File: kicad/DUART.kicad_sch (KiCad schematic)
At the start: 1 part

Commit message: Lot of stuff. Memmory decoder in GAL Added README for Digital Updated sketch for Arduino
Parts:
- added C? (x2): C, symbol Device:C
- added U?: 74LS245, symbol 74xx:74LS245
- added U?: 74LS244, symbol 74xx:74LS244
- added Y?: Crystal, symbol Device:Crystal
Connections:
- net RS1: now reaches U?.1 (RS1)
- net RS1: now also U?.3 (RS2), U?.5 (RS3), U?.6 (RS4), U?.12 (O3a), U?.14 (O2a), U?.16 (O1a), U?.18 (O0a)
- net D1: now reaches U?.16 (D1)
- net D1: now also U?.8 (A6)
- net D3: now reaches U?.17 (D3)
- net D3: now also U?.6 (A4)
- net D5: now reaches U?.18 (D5)
- net D5: now also U?.4 (A2)
- net D7: now reaches U?.19 (D7)
- net D7: now also U?.2 (A0)
- net D6: now reaches U?.22 (D6)
- net D6: now also U?.3 (A1)
- net D4: now reaches U?.23 (D4)
- net D4: now also U?.5 (A3)
- net D2: now reaches U?.24 (D2)
- net D2: now also U?.7 (A5)
- net D0: now reaches U?.25 (D0)
- net D0: now also U?.9 (A7)
- net at U?.32 (X1/CLK): now also C?.2, Y?.1
- net at U?.33 (X2): now also C?.2, Y?.2
- net VCC: now reaches U?.40 (VCC)
- net VCC: now also U?.19 (OEb), U?.20 (VCC), U?.20 (VCC)
- net DUART_R/W: now reaches U?.8 (R/W)
- new net GND: C?.1, C?.1, U?.10 (GND)

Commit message: KiCad updates
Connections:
- net DUART_R/W is gone; now on net ~{ODDWRITE}: U?.8 (R/W)
- net GND: now also U?.11 (I0b), U?.13 (I1b), U?.15 (I2b), U?.17 (I3b), U?.3 (O3b), U?.5 (O2b), U?.7 (O1b), U?.9 (O0b)
- net ~{DUARTSEL}: now reaches U?.35 (CS)
- net ~{DUARTSEL}: now also U?.1 (OEa), U?.19 (CE)
- net ~{ODDWRITE}: now reaches U?.1 (A->B)
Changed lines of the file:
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@@
 (kicad_sch (version 20211123) (generator eeschema)
   (paper "A4")
+  (junction (at 38.1 134.62) (diameter 0) (color 0 0 0 0)
+  )
+  (junction (at 38.1 132.08) (diameter 0) (color 0 0 0 0)
+  )
+  (junction (at 71.12 132.08) (diameter 0) (color 0 0 0 0)
+  )
   (junction (at 93.98 44.45) (diameter 0) (color 0 0 0 0)
   )
+  (junction (at 38.1 137.16) (diameter 0) (color 0 0 0 0)
+  )
   (junction (at 104.14 44.45) (diameter 0) (color 0 0 0 0)
   )
+  (junction (at 71.12 134.62) (diameter 0) (color 0 0 0 0)
+  )
+  (junction (at 71.12 137.16) (diameter 0) (color 0 0 0 0)
+  )
   (bus_entry (at 105.41 71.12) (size 2.54 -2.54)
     (stroke (width 0) (type default) (color 0 0 0 0))
@@
     (stroke (width 0) (type default) (color 0 0 0 0))
   )
+  (wire (pts (xy 67.31 137.16) (xy 71.12 137.16))
+    (stroke (width 0) (type default) (color 0 0 0 0))
+  )
   (bus (pts (xy 105.41 93.98) (xy 105.41 91.44))
     (stroke (width 0) (type default) (color 0 0 0 0))
   )
+  (wire (pts (xy 71.12 134.62) (xy 71.12 137.16))
+    (stroke (width 0) (type default) (color 0 0 0 0))
+  )
+  (wire (pts (xy 71.12 129.54) (xy 71.12 132.08))
+    (stroke (width 0) (type default) (color 0 0 0 0))
+  )
   (wire (pts (xy 107.95 66.04) (xy 116.84 66.04))
     (stroke (width 0) (type default) (color 0 0 0 0))
@@
     (stroke (width 0) (type default) (color 0 0 0 0))
   )
+  (wire (pts (xy 67.31 134.62) (xy 71.12 134.62))
+    (stroke (width 0) (type default) (color 0 0 0 0))
+  )
   (bus (pts (xy 105.41 73.66) (xy 105.41 76.2))
     (stroke (width 0) (type default) (color 0 0 0 0))
@@
     (stroke (width 0) (type default) (color 0 0 0 0))
   )
+  (wire (pts (xy 67.31 132.08) (xy 71.12 132.08))
+    (stroke (width 0) (type default) (color 0 0 0 0))
+  )
+  (wire (pts (xy 71.12 137.16) (xy 72.39 137.16))
+    (stroke (width 0) (type default) (color 0 0 0 0))
+  )
   (bus (pts (xy 105.41 68.58) (xy 105.41 71.12))
     (stroke (width 0) (type default) (color 0 0 0 0))
@@
     (stroke (width 0) (type default) (color 0 0 0 0))
   )
-  (wire (pts (xy 107.95 101.6) (xy 116.84 101.6))
+  (wire (pts (xy 38.1 134.62) (xy 38.1 137.16))
     (stroke (width 0) (type default) (color 0 0 0 0))
   )
@@
     (stroke (width 0) (type default) (color 0 0 0 0))
   )
+  (wire (pts (xy 36.83 137.16) (xy 38.1 137.16))
+    (stroke (width 0) (type default) (color 0 0 0 0))
+  )
   (bus (pts (xy 105.41 71.12) (xy 105.41 73.66))
     (stroke (width 0) (type default) (color 0 0 0 0))
@@
     (stroke (width 0) (type default) (color 0 0 0 0))
   )
+  (wire (pts (xy 38.1 134.62) (xy 41.91 134.62))
+    (stroke (width 0) (type default) (color 0 0 0 0))
+  )
   (wire (pts (xy 104.14 25.4) (xy 104.14 29.21))
     (stroke (width 0) (type default) (color 0 0 0 0))
@@
     (stroke (width 0) (type default) (color 0 0 0 0))
   )
+  (wire (pts (xy 67.31 129.54) (xy 71.12 129.54))
+    (stroke (width 0) (type default) (color 0 0 0 0))
+  )
   (bus (pts (xy 78.74 121.92) (xy 78.74 124.46))
     (stroke (width 0) (type default) (color 0 0 0 0))
   )
+  (wire (pts (xy 38.1 137.16) (xy 41.91 137.16))
+    (stroke (width 0) (type default) (color 0 0 0 0))
+  )
   (wire (pts (xy 93.98 44.45) (xy 93.98 58.42))
     (stroke (width 0) (type default) (color 0 0 0 0))
   )
+  (wire (pts (xy 38.1 132.08) (xy 41.91 132.08))
+    (stroke (width 0) (type default) (color 0 0 0 0))
+  )
   (bus (pts (xy 78.74 68.58) (xy 78.74 66.04))
     (stroke (width 0) (type default) (color 0 0 0 0))
   )
+  (wire (pts (xy 38.1 132.08) (xy 38.1 134.62))
+    (stroke (width 0) (type default) (color 0 0 0 0))
+  )
   (wire (pts (xy 104.14 44.45) (xy 104.14 55.88))
     (stroke (width 0) (type default) (color 0 0 0 0))
@@
     (stroke (width 0) (type default) (color 0 0 0 0))
   )
+  (wire (pts (xy 38.1 129.54) (xy 38.1 132.08))
+    (stroke (width 0) (type default) (color 0 0 0 0))
+  )
   (wire (pts (xy 107.95 76.2) (xy 116.84 76.2))
     (stroke (width 0) (type default) (color 0 0 0 0))
   )
+  (wire (pts (xy 41.91 129.54) (xy 38.1 129.54))
+    (stroke (width 0) (type default) (color 0 0 0 0))
+  )
   (bus (pts (xy 105.41 96.52) (xy 105.41 93.98))
     (stroke (width 0) (type default) (color 0 0 0 0))
@@
     (stroke (width 0) (type default) (color 0 0 0 0))
   )
+  (wire (pts (xy 71.12 132.08) (xy 71.12 134.62))
+    (stroke (width 0) (type default) (color 0 0 0 0))
+  )
   (wire (pts (xy 104.14 44.45) (xy 102.87 44.45))
     (stroke (width 0) (type default) (color 0 0 0 0))
@@
     )
   )
-  (global_label "DUART_R{slash}W" (shape input) (at 107.95 101.6 180) (fields_autoplaced)
+  (global_label "~{DUARTSEL}" (shape input) (at 116.84 99.06 180) (fields_autoplaced)
     (effects (font (size 1.27 1.27)) (justify right))
-    (property "Intersheet References" "${INTERSHEET_REFS}" (id 0) (at 94.5907 101.5206 0)
+    (property "Intersheet References" "${INTERSHEET_REFS}" (id 0) (at 105.1136 99.1394 0)
       (effects (font (size 1.27 1.27)) (justify right) hide)
     )
@@
     )
   )
+  (global_label "~{ODDWRITE}" (shape input) (at 116.84 101.6 180) (fields_autoplaced)
+    (effects (font (size 1.27 1.27)) (justify right))
+    (property "Intersheet References" "${INTERSHEET_REFS}" (id 0) (at 105.1136 101.5206 0)
+      (effects (font (size 1.27 1.27)) (justify right) hide)
+    )
+  )
   (global_label "D6" (shape bidirectional) (at 35.56 78.74 0) (fields_autoplaced)
     (effects (font (size 1.27 1.27)) (justify left))
@@
     )
   )
+  (global_label "~{DUARTSEL}" (shape input) (at 41.91 142.24 180) (fields_autoplaced)
+    (effects (font (size 1.27 1.27)) (justify right))
+    (property "Intersheet References" "${INTERSHEET_REFS}" (id 0) (at 30.1836 142.3194 0)
+      (effects (font (size 1.27 1.27)) (justify right) hide)
+    )
+  )
+  (global_label "~{DUARTSEL}" (shape input) (at 67.31 55.88 0) (fields_autoplaced)
+    (effects (font (size 1.27 1.27)) (justify left))
+    (property "Intersheet References" "${INTERSHEET_REFS}" (id 0) (at 79.0364 55.8006 0)
+      (effects (font (size 1.27 1.27)) (justify left) hide)
+    )
+  )
   (global_label "A4" (shape output) (at 35.56 127 0) (fields_autoplaced)
     (effects (font (size 1.27 1.27)) (justify left))
     (property "Intersheet References" "${INTERSHEET_REFS}" (id 0) (at 40.2712 126.9206 0)
+      (effects (font (size 1.27 1.27)) (justify left) hide)
+    )
+  )
+  (global_label "~{ODDWRITE}" (shape input) (at 67.31 58.42 0) (fields_autoplaced)
+    (effects (font (size 1.27 1.27)) (justify left))
+    (property "Intersheet References" "${INTERSHEET_REFS}" (id 0) (at 79.0364 58.4994 0)
       (effects (font (size 1.27 1.27)) (justify left) hide)
     )
@@
     (pin "1")
   )
-  (symbol (lib_id "power:GND") (at 95.25 139.7 0) (unit 1)
-    (in_bom yes) (on_board yes) (fields_autoplaced)
-    (property "Reference" "#PWR?" (id 0) (at 95.25 146.05 0)
-      (effects (font (size 1.27 1.27)) hide)
-    )
-    (property "Value" "GND" (id 1) (at 95.25 144.78 0))
-    (property "Footprint" "" (id 2) (at 95.25 139.7 0)
-      (effects (font (size 1.27 1.27)) hide)
-    )
-    (property "Datasheet" "" (id 3) (at 95.25 139.7 0)
+  (symbol (lib_id "power:GND") (at 36.83 137.16 270) (unit 1)
+    (in_bom yes) (on_board yes) (fields_autoplaced)
+    (property "Reference" "#PWR?" (id 0) (at 30.48 137.16 0)
+      (effects (font (size 1.27 1.27)) hide)
+    )
+    (property "Value" "GND" (id 1) (at 33.02 137.1599 90)
+      (effects (font (size 1.27 1.27)) (justify right))
+    )
+    (property "Footprint" "" (id 2) (at 36.83 137.16 0)
+      (effects (font (size 1.27 1.27)) hide)
+    )
+    (property "Datasheet" "" (id 3) (at 36.83 137.16 0)
       (effects (font (size 1.27 1.27)) hide)
     )
@@
       (effects (font (size 1.27 1.27)) hide)
     )
+    (pin "1")
+  )
+  (symbol (lib_id "power:GND") (at 72.39 137.16 90) (unit 1)
+    (in_bom yes) (on_board yes) (fields_autoplaced)
+    (property "Reference" "#PWR?" (id 0) (at 78.74 137.16 0)
+      (effects (font (size 1.27 1.27)) hide)
+    )
+    (property "Value" "GND" (id 1) (at 76.2 137.1599 90)
+      (effects (font (size 1.27 1.27)) (justify right))
+    )
+    (property "Footprint" "" (id 2) (at 72.39 137.16 0)
+      (effects (font (size 1.27 1.27)) hide)
+    )
+    (property "Datasheet" "" (id 3) (at 72.39 137.16 0)
+      (effects (font (size 1.27 1.27)) hide)
+    )

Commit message: started with pcb
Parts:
- added J1: Conn_01x06_Male, Connector_PinHeader_2.54mm:PinHeader_1x06_P2.54mm_Vertical, symbol Connector:Conn_01x06_Male
- C12, C13: renamed from C?; footprint (none) -> Capacitor_THT:CP_Radial_D8.0mm_P5.00mm
- U10, U9: renamed from U?; footprint (none) -> Package_DIP:DIP-20_W7.62mm_Socket
- U11: renamed from U?; footprint (none) -> Package_DIP:DIP-40_W15.24mm_Socket
- Y1: renamed from Y?; footprint (none) -> Crystal:Crystal_HC18-U_Vertical
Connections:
- net A1: now also U10.2 (I0a)
- net A2: now also U10.4 (I1a)
- net A3: now also U10.6 (I2a)
- net A4: now also U10.8 (I3a)
- net D0: now also U9.11 (B7)
- net D1: now also U9.12 (B6)
- net D2: now also U9.13 (B5)
- net D3: now also U9.14 (B4)
- net D4: now also U9.15 (B3)
- net D5: now also U9.16 (B2)
- net D6: now also U9.17 (B1)
- net D7: now also U9.18 (B0)
- net GND: now also U11.20 (GND), U9.10 (GND), J1.1 (Pin_1); no longer U10.11 (I0b), U10.13 (I1b), U10.15 (I2b), U10.17 (I3b), U10.3 (O3b), U10.5 (O2b), U10.7 (O1b), U10.9 (O0b)
- net TXDA: now reaches U11.30 (TXDA)
- net TXDA: now also J1.5 (Pin_5)
- net RXDA: now reaches U11.31 (RXDA)
- net RXDA: now also J1.4 (Pin_4)
- net /RESET: now reaches U11.34 (RESET)
- no-connect marks 0 -> 29
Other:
- title: (none) -> Mats Brorson 68010 SBC DUART 68681

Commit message: Update footprint
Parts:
- C12, C13: footprint Capacitor_THT:CP_Radial_D8.0mm_P5.00mm -> Capacitor_THT:CP_Radial_D5.0mm_P2.50mm
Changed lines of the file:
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@@
     (property "Reference" "C12" (id 0) (at 101.6 33.02 90))
     (property "Value" "C" (id 1) (at 99.06 33.02 90))
-    (property "Footprint" "Capacitor_THT:CP_Radial_D8.0mm_P5.00mm" (id 2) (at 94.9452 36.83 0)
+    (property "Footprint" "Capacitor_THT:CP_Radial_D5.0mm_P2.50mm" (id 2) (at 94.9452 36.83 0)
       (effects (font (size 1.27 1.27)) hide)
     )
@@
     (property "Reference" "C13" (id 0) (at 111.76 33.02 90))
     (property "Value" "C" (id 1) (at 109.22 33.02 90))
-    (property "Footprint" "Capacitor_THT:CP_Radial_D8.0mm_P5.00mm" (id 2) (at 105.1052 36.83 0)
-      (effects (font (size 1.27 1.27)) hide)
-    )
+    (property "Footprint" "Capacitor_THT:CP_Radial_D5.0mm_P2.50mm" (id 2) (at 105.1052 36.83 0)
+      (effects (font (size 1.27 1.27)) hide)
+    )

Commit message: cleanup
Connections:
- no-connect marks 29 -> 28

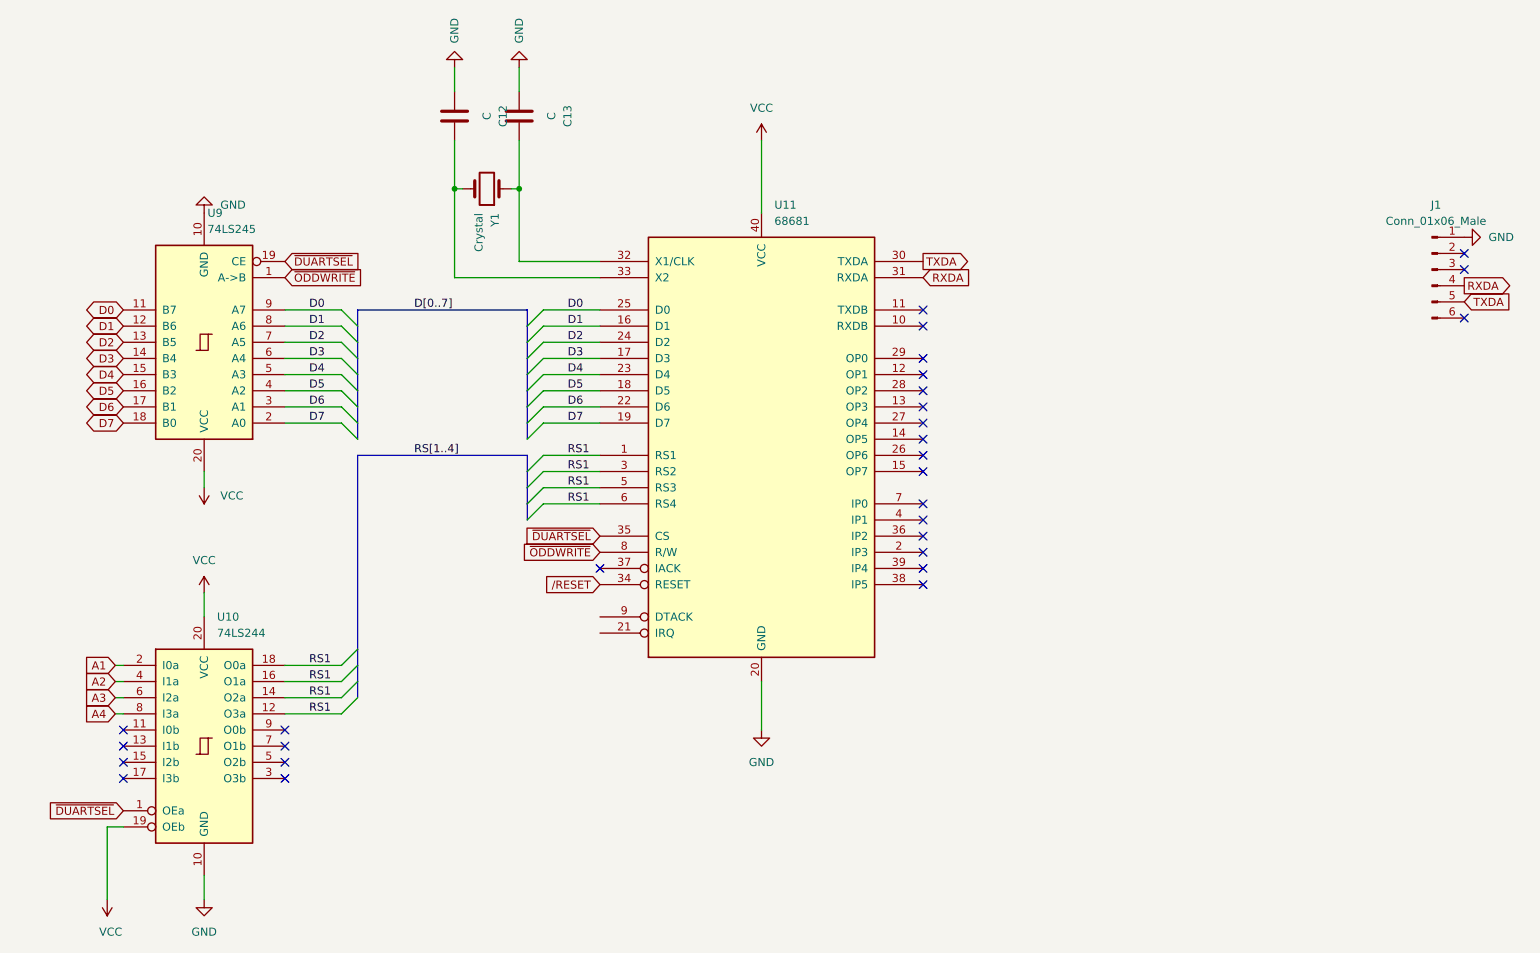
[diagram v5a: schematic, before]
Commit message: New decoding and GALs
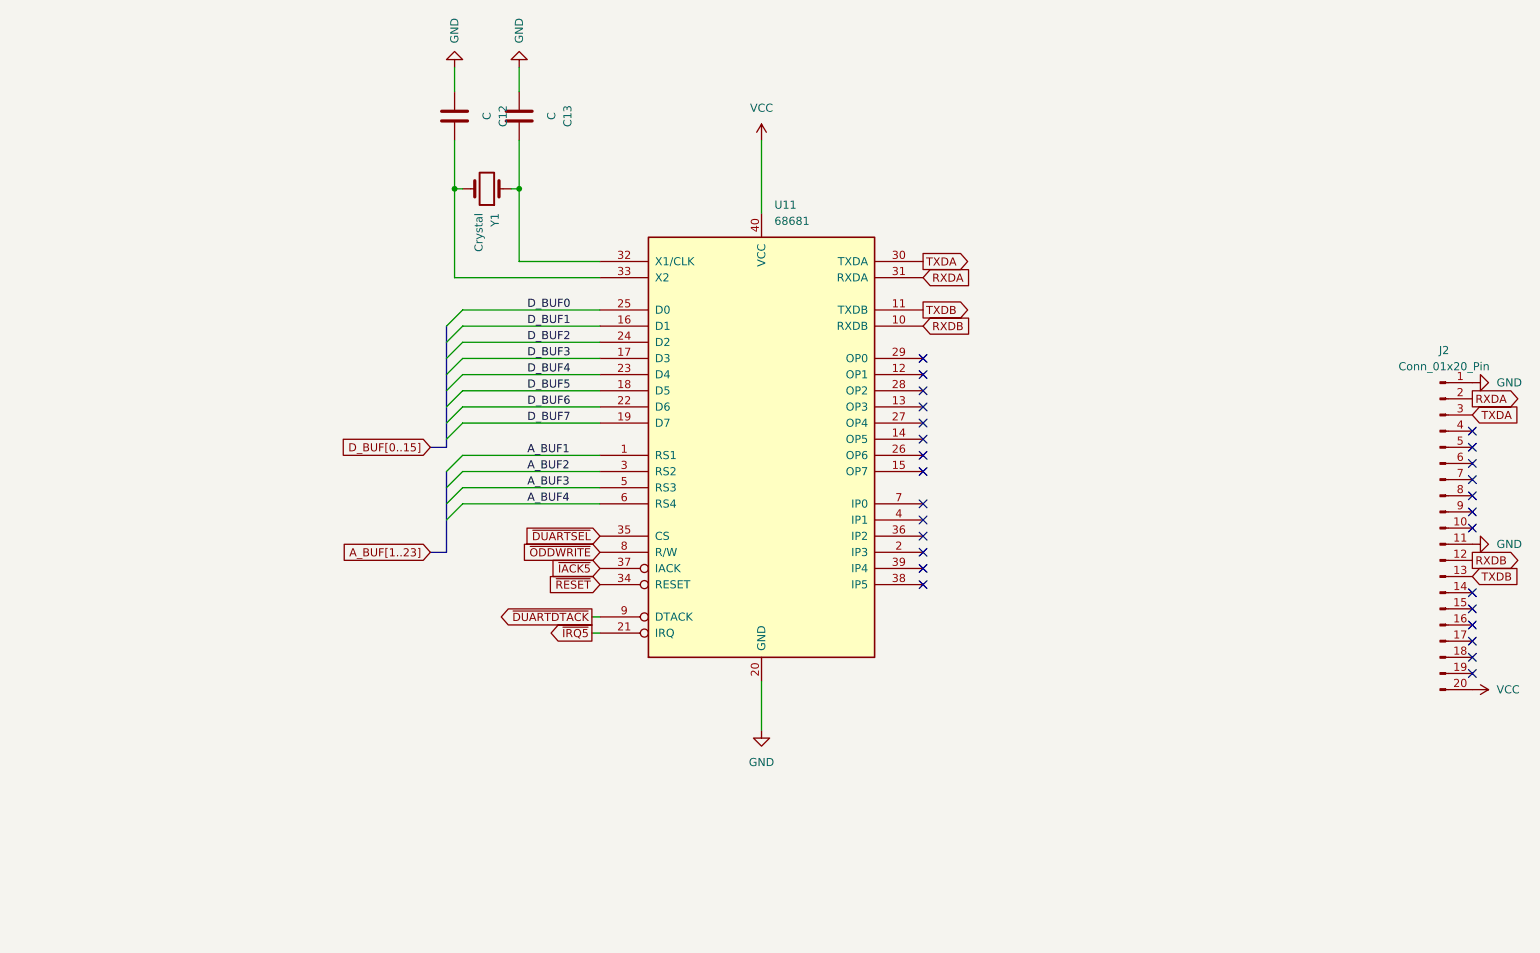
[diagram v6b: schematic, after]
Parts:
- removed J1: Conn_01x06_Male, Connector_PinHeader_2.54mm:PinHeader_1x06_P2.54mm_Vertical, symbol Connector:Conn_01x06_Male
- removed U10: 74LS244, Package_DIP:DIP-20_W7.62mm_Socket, symbol 74xx:74LS244
- removed U9: 74LS245, Package_DIP:DIP-20_W7.62mm_Socket, symbol 74xx:74LS245
- added J2: Conn_01x20_Pin, symbol Connector:Conn_01x20_Pin
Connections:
- net GND: now also J2.1 (Pin_1), J2.11 (Pin_11)
- net RXDA: now also J2.2 (Pin_2)
- net TXDA: now also J2.3 (Pin_3)
- net VCC: now also J2.20 (Pin_20)
- net RXDB: now reaches U11.10 (RXDB)
- net RXDB: now also J2.12 (Pin_12)
- net TXDB: now reaches U11.11 (TXDB)
- net TXDB: now also J2.13 (Pin_13)
- net ~{IRQ5}: now reaches U11.21 (IRQ)
- net ~{IACK5}: now reaches U11.37 (IACK)
- net ~{DUARTDTACK}: now reaches U11.9 (DTACK)
- net D0 renamed D_BUF0
- net D1 renamed D_BUF1
- net D2 renamed D_BUF2
- net D3 renamed D_BUF3
- net D4 renamed D_BUF4
- net D5 renamed D_BUF5
- net D6 renamed D_BUF6
- net D7 renamed D_BUF7
- removed net RS1: U11.1 (RS1), U11.3 (RS2), U11.5 (RS3), U11.6 (RS4)
- net /RESET renamed ~{RESET}
- new net A_BUF1: U11.1 (RS1)
- new net A_BUF2: U11.3 (RS2)
- new net A_BUF3: U11.5 (RS3)
- new net A_BUF4: U11.6 (RS4)
- no-connect marks 28 -> 27
